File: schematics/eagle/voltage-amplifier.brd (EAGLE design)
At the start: 46.5 x 25.5 mm, 15 parts, among them Q1 2N3904, Q2 2N3904, Q3 2N3904, Q4 2N3904

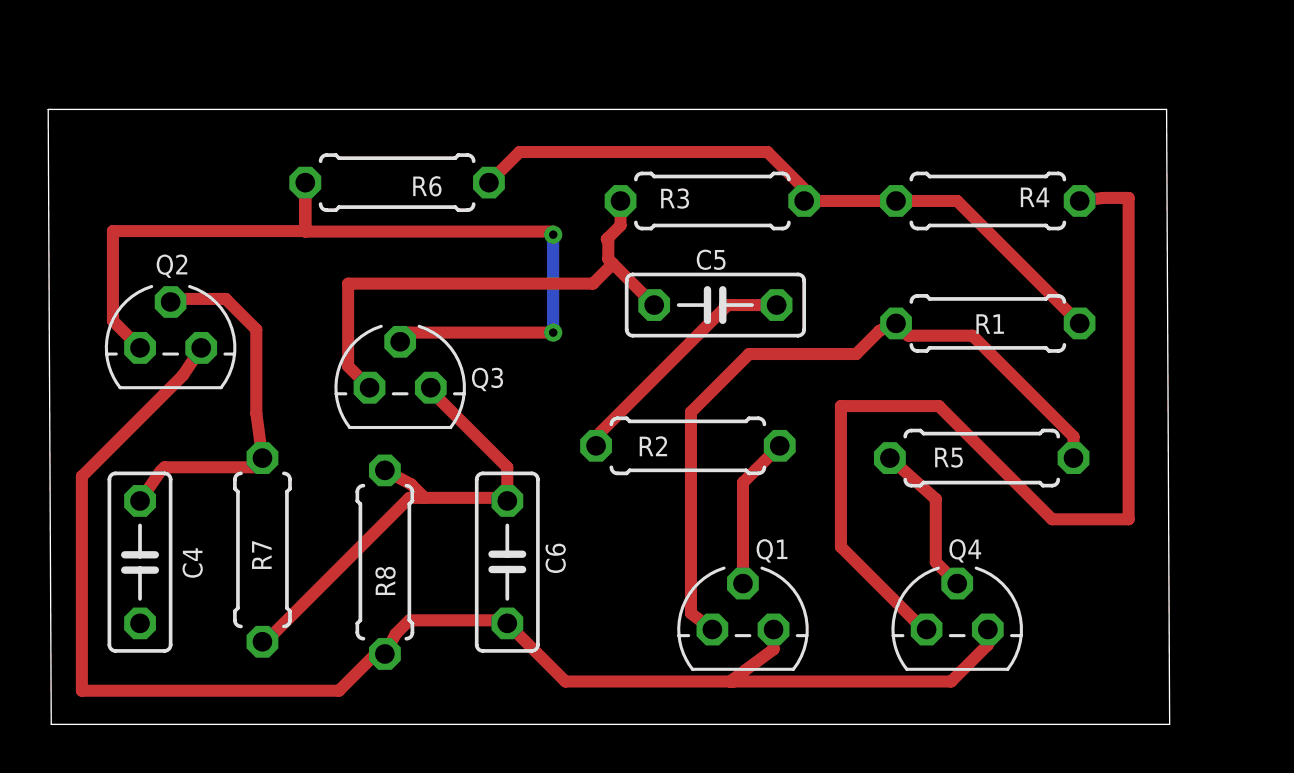
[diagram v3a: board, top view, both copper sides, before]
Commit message: Changed package for the big resistances
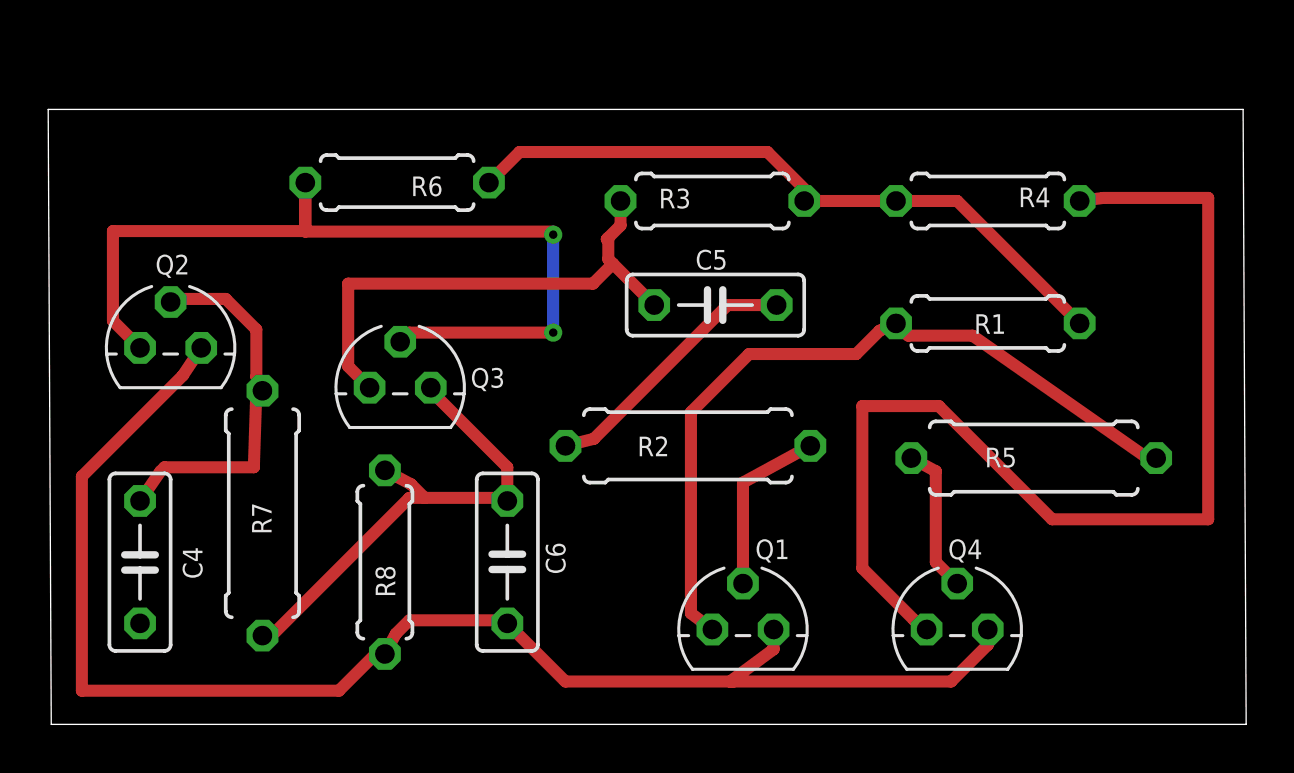
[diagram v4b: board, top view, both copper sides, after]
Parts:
- R2, R5, R7: device sym-toh:0207/7 -> sym-toh:0309/10
- moved R5 2.16 mm to (40.8, 11.0)
- moved R7 1.52 mm to (8.76, 8.76)
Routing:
- net VOUT: track 40.0 -> 45.4 mm
- net N$3: track 29.6 -> 32.0 mm
- net N$7: track 6.35 -> 7.37 mm
- net N$6: track 10.2 -> 11.1 mm
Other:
- board size 46.5 x 25.5 mm -> 49.7 x 25.5 mm
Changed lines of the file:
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@@
 <board>
 <plain>
-<wire x1="0" y1="0" x2="46.406" y2="0" width="0" layer="20"/>
-<wire x1="46.406" y1="0" x2="46.279" y2="25.517" width="0" layer="20"/>
-<wire x1="46.279" y1="25.517" x2="-0.127" y2="25.517" width="0" layer="20"/>
+<wire x1="0" y1="0" x2="49.581" y2="0" width="0" layer="20"/>
+<wire x1="49.581" y1="0" x2="49.454" y2="25.517" width="0" layer="20"/>
+<wire x1="49.454" y1="25.517" x2="-0.127" y2="25.517" width="0" layer="20"/>
 <wire x1="-0.127" y1="25.517" x2="0" y2="0" width="0" layer="20"/>
 </plain>
@@
 <attribute name="VALUE" x="41.148" y="17.1958" size="1.27" layer="27" ratio="10" rot="R180"/>
 </element>
-<element name="R2" library="sym-toh" package="0207/7" value="100k" x="26.416" y="11.557" smashed="yes" rot="R180">
+<element name="R2" library="sym-toh" package="0309/10" value="100k" x="26.416" y="11.557" smashed="yes" rot="R180">
 <attribute name="NAME" x="25.654" y="11.938" size="0.8128" layer="25" ratio="10" rot="R180"/>
 <attribute name="VALUE" x="28.702" y="12.1158" size="1.27" layer="27" ratio="10" rot="R180"/>
@@
 <attribute name="VALUE" x="36.576" y="21.1582" size="1.27" layer="27" ratio="10"/>
 </element>
-<element name="R5" library="sym-toh" package="0207/7" value="100k" x="38.608" y="11.049" smashed="yes">
-<attribute name="NAME" x="36.576" y="10.668" size="0.8128" layer="25" ratio="10"/>
-<attribute name="VALUE" x="36.322" y="10.4902" size="1.27" layer="27" ratio="10"/>
+<element name="R5" library="sym-toh" package="0309/10" value="100k" x="40.767" y="11.049" smashed="yes">
+<attribute name="NAME" x="38.735" y="10.668" size="0.8128" layer="25" ratio="10"/>
+<attribute name="VALUE" x="38.481" y="10.4902" size="1.27" layer="27" ratio="10"/>
 </element>
 <element name="R6" library="sym-toh" package="0207/7" value="4.7k" x="14.351" y="22.479" smashed="yes" rot="R180">
@@
 <attribute name="VALUE" x="16.637" y="23.0378" size="1.27" layer="27" ratio="10" rot="R180"/>
 </element>
-<element name="R7" library="sym-toh" package="0207/7" value="100k" x="8.763" y="7.239" smashed="yes" rot="R90">
-<attribute name="NAME" x="9.144" y="6.35" size="0.8128" layer="25" ratio="10" rot="R90"/>
-<attribute name="VALUE" x="9.3218" y="4.953" size="1.27" layer="27" ratio="10" rot="R90"/>
+<element name="R7" library="sym-toh" package="0309/10" value="100k" x="8.763" y="8.763" smashed="yes" rot="R90">
+<attribute name="NAME" x="9.144" y="7.874" size="0.8128" layer="25" ratio="10" rot="R90"/>
+<attribute name="VALUE" x="9.3218" y="6.477" size="1.27" layer="27" ratio="10" rot="R90"/>
 </element>
 <element name="R8" library="sym-toh" package="0207/7" value="4.7k" x="13.843" y="6.731" smashed="yes" rot="R270">
@@
 <contactref element="Q4" pad="2"/>
 <contactref element="R5" pad="1"/>
-<wire x1="34.798" y1="11.049" x2="36.703" y2="9.34810625" width="0.5" layer="1"/>
+<wire x1="35.687" y1="11.049" x2="36.703" y2="10.5047125" width="0.5" layer="1"/>
 <wire x1="36.703" y1="6.731" x2="37.592" y2="5.842" width="0.5" layer="1"/>
-<wire x1="36.703" y1="9.34810625" x2="36.703" y2="6.731" width="0.5" layer="1"/>
+<wire x1="36.703" y1="10.5047125" x2="36.703" y2="6.731" width="0.5" layer="1"/>
 </signal>
 <signal name="V+">
@@
 <wire x1="26.543" y1="4.6074" x2="27.432" y2="3.937" width="0.5" layer="1"/>
 <wire x1="34.370209375" y1="16.336209375" x2="35.052" y2="16.637" width="0.5" layer="1"/>
-<wire x1="42.418" y1="11.049" x2="42.418" y2="11.938" width="0.5" layer="1"/>
-<wire x1="42.418" y1="11.938" x2="38.227" y2="16.129" width="0.5" layer="1"/>
+<wire x1="45.847" y1="11.049" x2="45.48414375" y2="11.049" width="0.5" layer="1"/>
+<wire x1="45.48414375" y1="11.049" x2="38.227" y2="16.129" width="0.5" layer="1"/>
 <wire x1="38.227" y1="16.129" x2="35.56" y2="16.129" width="0.5" layer="1"/>
 <wire x1="35.56" y1="16.129" x2="35.052" y2="16.637" width="0.5" layer="1"/>
@@
 <contactref element="R4" pad="2"/>
 <contactref element="Q4" pad="3"/>
-<wire x1="32.766" y1="7.366" x2="35.805515625" y2="4.326484375" width="0.5" layer="1"/>
-<wire x1="32.766" y1="13.208" x2="32.766" y2="7.366" width="0.5" layer="1"/>
-<wire x1="36.83" y1="13.208" x2="32.766" y2="13.208" width="0.5" layer="1"/>
+<wire x1="33.655" y1="6.477" x2="35.805515625" y2="4.326484375" width="0.5" layer="1"/>
+<wire x1="33.655" y1="13.208" x2="33.655" y2="6.477" width="0.5" layer="1"/>
+<wire x1="36.83" y1="13.208" x2="33.655" y2="13.208" width="0.5" layer="1"/>
 <wire x1="41.529" y1="8.509" x2="36.83" y2="13.208" width="0.5" layer="1"/>
-<wire x1="44.704" y1="8.509" x2="41.529" y2="8.509" width="0.5" layer="1"/>
-<wire x1="44.704" y1="21.844" x2="44.704" y2="8.509" width="0.5" layer="1"/>
-<wire x1="43.646015625" y1="21.844" x2="44.704" y2="21.844" width="0.5" layer="1"/>
+<wire x1="48.006" y1="8.509" x2="41.529" y2="8.509" width="0.5" layer="1"/>
+<wire x1="48.006" y1="21.844" x2="48.006" y2="8.509" width="0.5" layer="1"/>
+<wire x1="43.646015625" y1="21.844" x2="48.006" y2="21.844" width="0.5" layer="1"/>
 <wire x1="35.805515625" y1="4.326484375" x2="36.322" y2="3.937" width="0.5" layer="1"/>
 <wire x1="42.672" y1="21.717" x2="43.646015625" y2="21.844" width="0.5" layer="1"/>
@@
 <wire x1="28.067" y1="17.399" x2="22.51860625" y2="11.85060625" width="0.5" layer="1"/>
 <wire x1="30.099" y1="17.399" x2="28.067" y2="17.399" width="0.5" layer="1"/>
-<wire x1="22.51860625" y1="11.85060625" x2="22.606" y2="11.557" width="0.5" layer="1"/>
+<wire x1="22.51860625" y1="11.85060625" x2="21.336" y2="11.557" width="0.5" layer="1"/>
 </signal>
 <signal name="N$7">
 <contactref element="Q1" pad="2"/>
 <contactref element="R2" pad="1"/>
-<wire x1="30.226" y1="11.557" x2="28.702" y2="10.033" width="0.5" layer="1"/>
+<wire x1="31.496" y1="11.557" x2="28.702" y2="10.033" width="0.5" layer="1"/>
 <wire x1="28.702" y1="10.033" x2="28.702" y2="5.842" width="0.5" layer="1"/>
 </signal>
@@
 <contactref element="R7" pad="2"/>
 <wire x1="4.699" y1="10.668" x2="4.52994375" y2="10.49894375" width="0.5" layer="1"/>
-<wire x1="8.70969375" y1="10.668" x2="4.699" y2="10.668" width="0.5" layer="1"/>
+<wire x1="8.4064875" y1="10.668" x2="4.699" y2="10.668" width="0.5" layer="1"/>
 <wire x1="4.52994375" y1="10.49894375" x2="3.683" y2="9.271" width="0.5" layer="1"/>
-<wire x1="8.70969375" y1="10.668" x2="8.763" y2="11.049" width="0.5" layer="1"/>
+<wire x1="8.500525" y1="13.580525" x2="8.763" y2="13.843" width="0.5" layer="1"/>
+<wire x1="8.500525" y1="13.580525" x2="8.4064875" y2="10.668" width="0.5" layer="1"/>
 <wire x1="7.239" y1="17.653" x2="5.397465625" y2="17.653" width="0.5" layer="1"/>
 <wire x1="8.509" y1="16.383" x2="7.239" y2="17.653" width="0.5" layer="1"/>
-<wire x1="8.509" y1="12.899159375" x2="8.509" y2="16.383" width="0.5" layer="1"/>
+<wire x1="8.509" y1="14.423159375" x2="8.509" y2="16.383" width="0.5" layer="1"/>
 <wire x1="5.397465625" y1="17.653" x2="4.953" y2="17.526" width="0.5" layer="1"/>
-<wire x1="8.509" y1="12.899159375" x2="8.763" y2="11.049" width="0.5" layer="1"/>
+<wire x1="8.509" y1="14.423159375" x2="8.763" y2="13.843" width="0.5" layer="1"/>
 </signal>
 <signal name="0">
@@
 <contactref element="R8" pad="1"/>
 <contactref element="C6" pad="2"/>
-<wire x1="14.859" y1="9.398" x2="9.040475" y2="3.579475" width="0.5" layer="1"/>
+<wire x1="14.859" y1="9.398" x2="9.236490625" y2="3.775490625" width="0.5" layer="1"/>
 <wire x1="15.494" y1="9.398" x2="14.859" y2="9.398" width="0.5" layer="1"/>
-<wire x1="9.040475" y1="3.579475" x2="8.763" y2="3.429" width="0.5" layer="1"/>
+<wire x1="9.236490625" y1="3.775490625" x2="8.763" y2="3.683" width="0.5" layer="1"/>
 <wire x1="15.494" y1="9.398" x2="14.928815625" y2="9.963184375" width="0.5" layer="1"/>
 <wire x1="14.928815625" y1="9.963184375" x2="13.843" y2="10.541" width="0.5" layer="1"/>
